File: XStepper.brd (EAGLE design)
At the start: 100.3 x 80 mm, 74 parts, among them Q2 16 MHZ

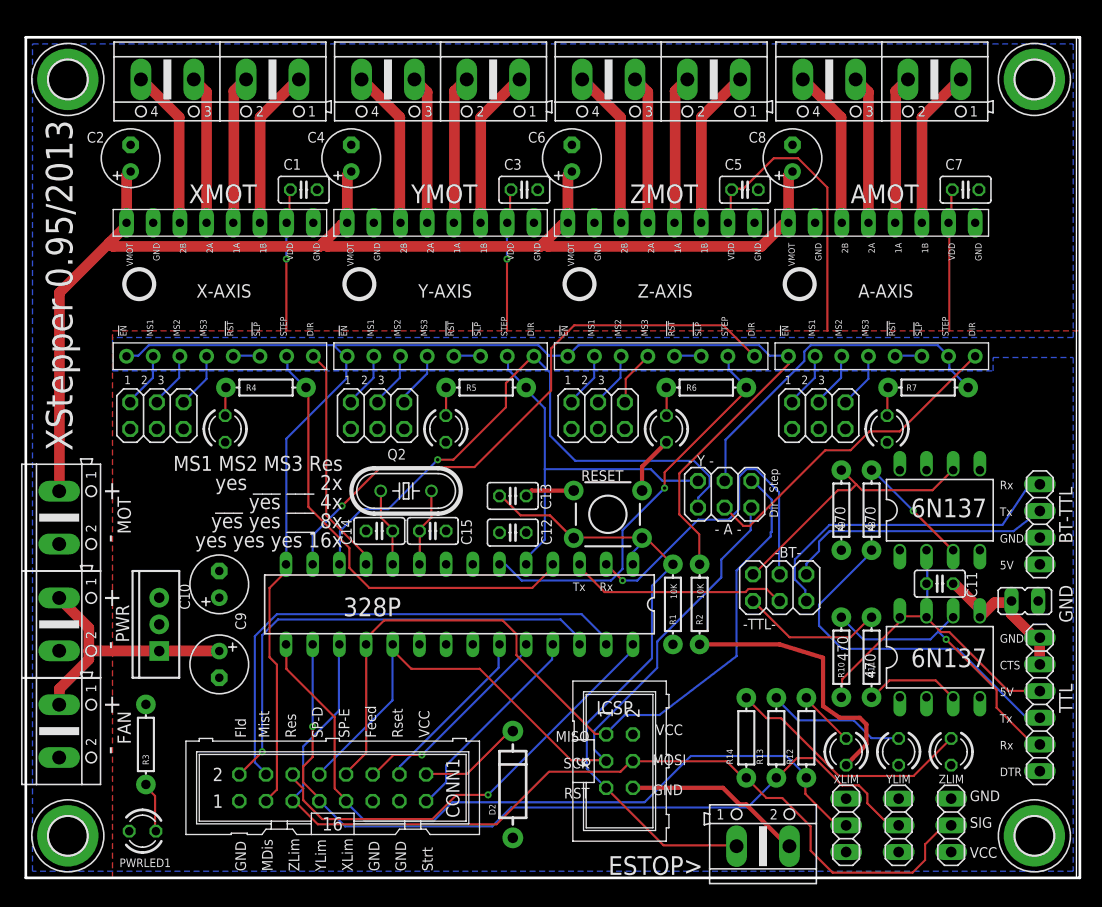
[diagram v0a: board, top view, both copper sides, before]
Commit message: Revert "- bugfix diode"
This reverts commit 7209bcb696f77dd3d5512bdf8e28195d083f39f3.
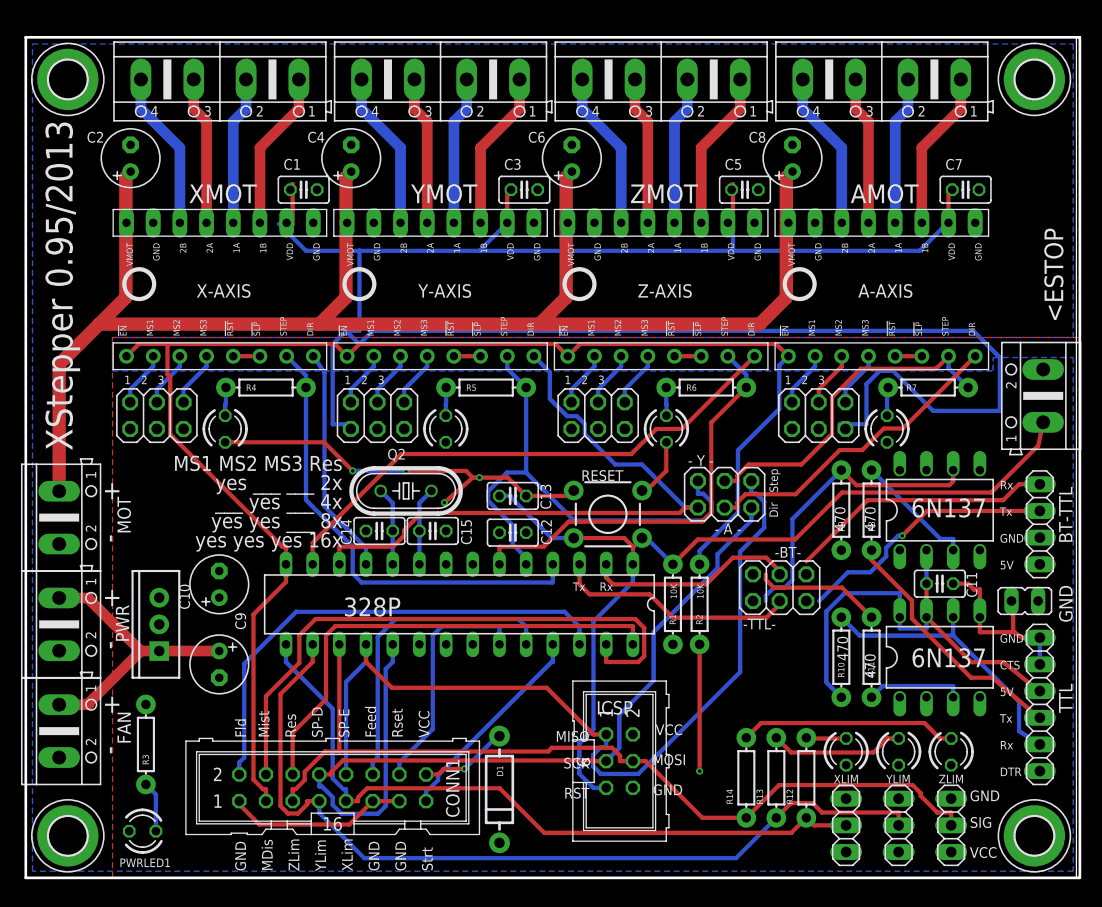
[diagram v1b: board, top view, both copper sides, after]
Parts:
- removed D2: (no value), SparkFun-DiscreteSemi:DIODE-1N4001
- removed ESTOP>: (no value), con-ptr500:AK500/2
- added <ESTOP: (no value), con-ptr500:AK500/2
- added D1: (no value), SparkFun-DiscreteSemi:DIODE-1N4001
- moved R12 3.81 mm to (74.3, 9.53)
- moved R13 3.81 mm to (71.4, 9.53)
- moved R14 3.81 mm to (68.6, 9.53)
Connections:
- net 5V: now also D1.C; no longer D2.A
- net GND: now also <ESTOP.2; no longer ESTOP>.2
- net N$45: now also D1.A; no longer D2.C
- net RESET: now also <ESTOP.1; no longer ESTOP>.1
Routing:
- net 5V: track 69.5 -> 201.2 mm, vias 2 -> 0
- net RESET: track 62.3 -> 88.5 mm
- net PWRMOT: track 120.6 -> 144.0 mm
- net GND: track 53.2 -> 74.4 mm, vias 0 -> 5
- net RXD: track 32.1 -> 19.9 mm, vias 1 -> 0
- net SPINDLE-DIR: track 71.4 -> 82.8 mm
- net Y-STEP: track 37.1 -> 48.3 mm
- net FEED-HOLD: track 20.1 -> 30.1 mm, vias 1 -> 0
- net USB_TXD: track 33.9 -> 24.0 mm
- net USB_5V: track 33.5 -> 43.4 mm
- net Z-STOP: track 91.4 -> 82.9 mm
- net COOLANT-MIST: track 49.4 -> 56.6 mm
- net G-RESET: track 16.4 -> 23.0 mm
- net BTTXD: track 31.2 -> 25.3 mm
- net SPINDLE-ENABLE: track 77.2 -> 82.6 mm
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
